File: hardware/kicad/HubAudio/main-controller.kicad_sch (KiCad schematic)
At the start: 17 parts, among them U10 W25Q128JVS, U17 24AA025E48, U35 74HC138

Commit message: Finalize I2C and SPI control architecture
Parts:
- added R75, R76, R94: 10K, Resistor_SMD:R_0805_2012Metric, symbol Device:R
- added R97: 33, Resistor_SMD:R_0805_2012Metric, symbol Device:R
- BOOT1, RESET1: PNM (none) -> TS3425UA-3x4x2.5-160
- C159, C65, C66, C68: PNM (none) -> GRM21BR71H104KA01L
- C45: PNM (none) -> GRM31CR71E106KA12L
- C64: footprint Capacitor_SMD:C_1206_3216Metric -> Capacitor_SMD:C_0805_2012Metric; PNM (none) -> GRM21BZ71A226ME15L
- C67: PNM (none) -> GCM21BR71E105KA56L
- R36, R44, R45: PNM (none) -> RC0805FR-074K7L
- R43: PNM (none) -> RC0805FR-0710KL
- U10: PNM (none) -> W25Q128JVS
- U11: value (none) -> ESP32-S31-WROOM-3; PNM (none) -> ESP32-S31-WROOM-3
- U17: value 24AA025E48 -> 24AA025E64; PNM (none) -> 24AA025E64
- U35: value 74HC138 -> 74HC138PW,118; footprint (none) -> Package_SO:TSSOP-16_4.4x5mm_P0.65mm; PNM (none) -> 74HC138PW,118
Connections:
- net 3V3_DIGITAL: now also R75.1, R76.1, R94.2
- net I2S_IN_ESP32_SDATA: now also R97.2; no longer U11.58 (GPIO48/ADC1_CH3_N)
- net SPI_CODEC_CS: now also U35.10 (~{Y5}); no longer U35.11 (~{Y4})
- net SPI_W25Q128_CS: now also R94.1
- net at U35.1 (A0): now also U11.44 (GPIO35)
- net SPI_UART_CS: now reaches U35.9 (~{Y6})
- net at U10.3 (IO2): now also R75.2
- net at U10.7 (IO3): now also R76.2
- net DEV_MAN_A_INT: now reaches U11.27 (SDIO_DATA0/GPIO20)
- net DEV_MAN_B_INT: now reaches U11.28 (SDIO_DATA1/GPIO21)
- net DEV_MAN_A_RESET: now reaches U11.29 (SDIO_DATA2/GPIO22)
- net DEV_MAN_B_RESET: now reaches U11.30 (SDIO_DATA3/GPIO23)
- net DEVICE_MANAGER_INT: no longer names the net of U11.22 (GPIO16)
- net DEVICE_MANAGER_RST: no longer names the net of U11.23 (GPIO17)
- net ETH_RST#: no longer names the net of U11.13 (GPIO7)
- net PCA_POWER_INT: no longer names the net of U11.17 (GPIO11)
- net SPI_DEV_MAN_CS renamed SPI_DEV_MAN_A_CS
- new net: R97.1, U11.58 (GPIO48/ADC1_CH3_N)
- new net SPI_DEV_MAN_B_CS: U35.11 (~{Y4})
- no-connect marks 2 -> 24

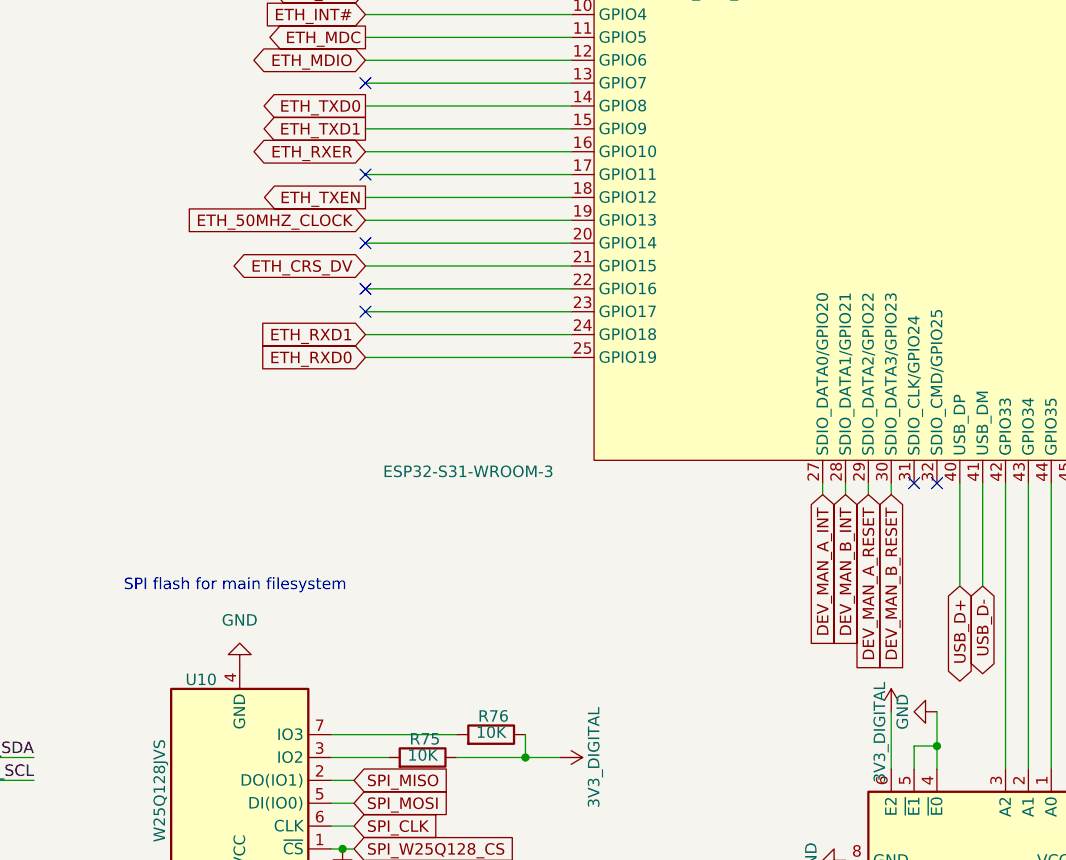
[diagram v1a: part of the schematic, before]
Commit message: Finalize HubAudio hardware architecture and PCB
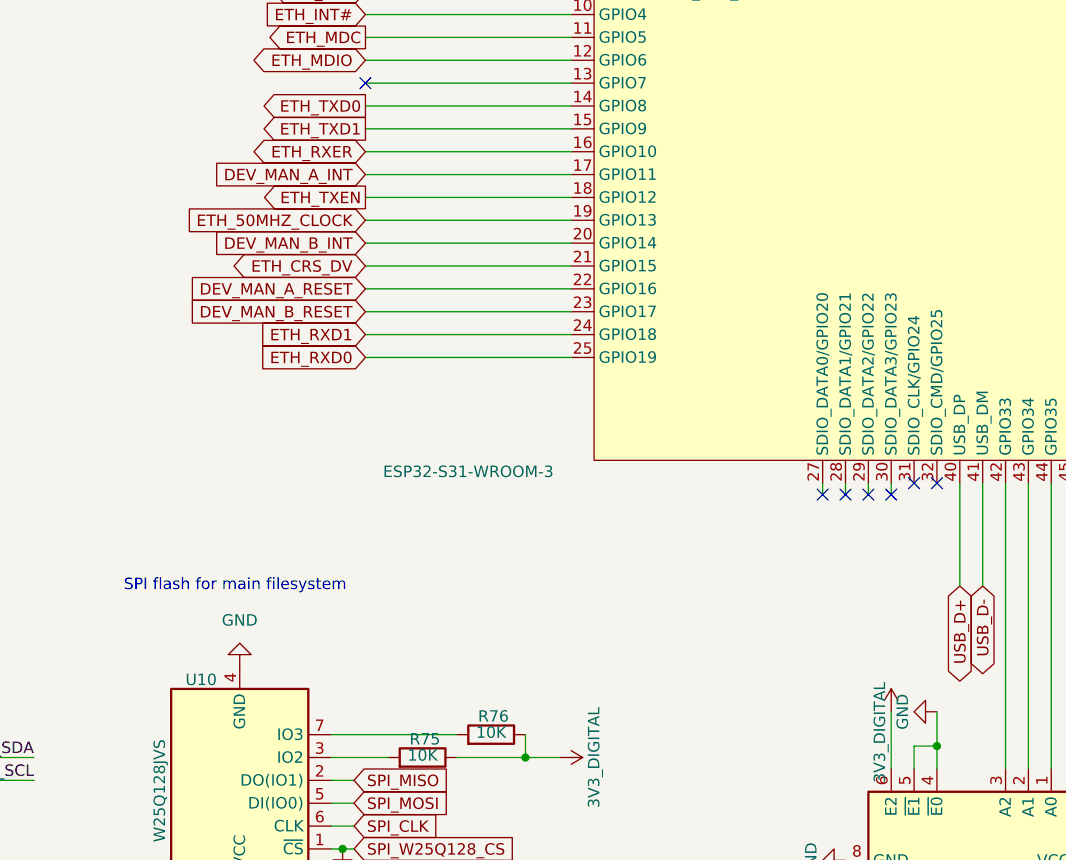
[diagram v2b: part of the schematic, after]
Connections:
- net DEV_MAN_A_INT: now also U11.17 (GPIO11); no longer U11.27 (SDIO_DATA0/GPIO20)
- net DEV_MAN_A_RESET: now also U11.22 (GPIO16); no longer U11.29 (SDIO_DATA2/GPIO22)
- net DEV_MAN_B_INT: now also U11.20 (GPIO14); no longer U11.28 (SDIO_DATA1/GPIO21)
- net DEV_MAN_B_RESET: now also U11.23 (GPIO17); no longer U11.30 (SDIO_DATA3/GPIO23)
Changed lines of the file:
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@@
+	)
+	(no_connect
+		(at 152.4 111.76)
 	)
 	(no_connect
@@
 	)
 	(no_connect
-		(at 96.52 76.2)
-	)
-	(no_connect
 		(at 232.41 60.96)
 	)
@@
 	)
 	(no_connect
-		(at 96.52 91.44)
+		(at 147.32 111.76)
 	)
 	(no_connect
@@
 	)
 	(no_connect
+		(at 175.26 110.49)
+	)
+	(no_connect
+		(at 205.74 50.8)
+	)
+	(no_connect
+		(at 157.48 110.49)
+	)
+	(no_connect
+		(at 154.94 111.76)
+	)
+	(no_connect
+		(at 205.74 43.18)
+	)
+	(no_connect
+		(at 205.74 48.26)
+	)
+	(no_connect
+		(at 149.86 111.76)
+	)
+	(no_connect
+		(at 96.52 53.34)
+	)
+	(no_connect
+		(at 205.74 71.12)
+	)
+	(no_connect
 		(at 96.52 66.04)
 	)
 	(no_connect
-		(at 96.52 83.82)
-	)
-	(no_connect
-		(at 175.26 110.49)
-	)
-	(no_connect
-		(at 205.74 50.8)
-	)
-	(no_connect
-		(at 157.48 110.49)
-	)
-	(no_connect
-		(at 205.74 43.18)
-	)
-	(no_connect
-		(at 205.74 48.26)
-	)
-	(no_connect
-		(at 96.52 53.34)
-	)
-	(no_connect
-		(at 205.74 71.12)
-	)
-	(no_connect
 		(at 232.41 53.34)
 	)
@@
 	(no_connect
 		(at 232.41 93.98)
-	)
-	(no_connect
-		(at 96.52 88.9)
 	)
 	(no_connect
@@
 		)
 	)
+	(global_label "DEV_MAN_A_INT"
+		(shape input)
+		(at 96.52 76.2 180)
+		(fields_autoplaced yes)
+		(effects
+			(font
+				(size 1.27 1.27)
+			)
+			(justify right)
+		)
+		(property "Intersheetrefs" "${INTERSHEET_REFS}"
+			(at 79.2624 76.2 0)
+			(hide yes)
+			(show_name no)
+			(do_not_autoplace no)
+			(effects
+				(font
+					(size 1.27 1.27)
+				)
+				(justify right)
+			)
+		)
+	)
+	(global_label "DEV_MAN_A_RESET"
+		(shape input)
+		(at 96.52 88.9 180)
+		(fields_autoplaced yes)
+		(effects
+			(font
+				(size 1.27 1.27)
+			)
+			(justify right)
+		)
+		(property "Intersheetrefs" "${INTERSHEET_REFS}"
+			(at 76.4202 88.9 0)
+			(hide yes)
+			(show_name no)
+			(do_not_autoplace no)
+			(effects
+				(font
+					(size 1.27 1.27)
+				)
+				(justify right)
+			)
+		)
+	)
 	(global_label "ETH_TXEN"
 		(shape output)
@@
 		)
 	)
+	(global_label "DEV_MAN_B_RESET"
+		(shape input)
+		(at 96.52 91.44 180)
+		(fields_autoplaced yes)
+		(effects
+			(font
+				(size 1.27 1.27)
+			)
+			(justify right)
+		)
+		(property "Intersheetrefs" "${INTERSHEET_REFS}"
+			(at 76.2388 91.44 0)
+			(hide yes)
+			(show_name no)
+			(do_not_autoplace no)
+			(effects
+				(font
+					(size 1.27 1.27)
+				)
+				(justify right)
+			)
+		)
+	)
 	(global_label "ETH_TXD0"
 		(shape output)
@@
 		)
 	)
-	(global_label "DEV_MAN_A_INT"
-		(shape input)
-		(at 147.32 111.76 270)
-		(fields_autoplaced yes)
-		(effects
-			(font
-				(size 1.27 1.27)
-			)
-			(justify right)
-		)
-		(property "Intersheetrefs" "${INTERSHEET_REFS}"
-			(at 147.32 129.0176 90)
-			(hide yes)
-			(show_name no)
-			(do_not_autoplace no)
-			(effects
-				(font
-					(size 1.27 1.27)
-				)
-				(justify right)
-			)
-		)
-	)
 	(global_label "SPI_ADAU1467_CS"
 		(shape output)
@@
 		)
 	)
-	(global_label "DEV_MAN_B_INT"
-		(shape input)
-		(at 149.86 111.76 270)
-		(fields_autoplaced yes)
-		(effects
-			(font
-				(size 1.27 1.27)
-			)
-			(justify right)
-		)
-		(property "Intersheetrefs" "${INTERSHEET_REFS}"
-			(at 149.86 129.199 90)
-			(hide yes)
-			(show_name no)
-			(do_not_autoplace no)
-			(effects
-				(font
-					(size 1.27 1.27)
-				)
-				(justify right)
-			)
-		)
-	)
 	(global_label "I2S_IN_ESP32_SDATA"
 		(shape bidirectional)
@@
 		)
 	)
-	(global_label "DEV_MAN_A_RESET"
+	(global_label "DEV_MAN_B_INT"
 		(shape input)
-		(at 152.4 111.76 270)
-		(fields_autoplaced yes)
-		(effects
-			(font
-				(size 1.27 1.27)
-			)
-			(justify right)
-		)
-		(property "Intersheetrefs" "${INTERSHEET_REFS}"
-			(at 152.4 131.8598 90)
+		(at 96.52 83.82 180)
+		(fields_autoplaced yes)
+		(effects
+			(font
+				(size 1.27 1.27)
+			)
+			(justify right)
+		)
+		(property "Intersheetrefs" "${INTERSHEET_REFS}"
+			(at 79.081 83.82 0)
 			(hide yes)
 			(show_name no)
@@
 			(hide yes)
 			(show_name no)
-			(do_not_autoplace no)
-			(effects
-				(font
-					(size 1.27 1.27)
-				)
-				(justify right)
-			)
-		)
-	)
-	(global_label "DEV_MAN_B_RESET"
-		(shape input)
-		(at 154.94 111.76 270)
-		(fields_autoplaced yes)
-		(effects
-			(font
-				(size 1.27 1.27)
-			)
-			(justify right)
-		)
-		(property "Intersheetrefs" "${INTERSHEET_REFS}"
-			(at 154.94 132.0412 90)
-			(hide yes)
-			(show_name no)
